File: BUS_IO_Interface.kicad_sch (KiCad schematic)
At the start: 20 parts, among them U26 DS28E83Q+T, U28 MAX31331TETB+, U29 MAX31725MTA+, U30 MAX31725MTA+, Y26 AB26T-32.768KHZ-6B

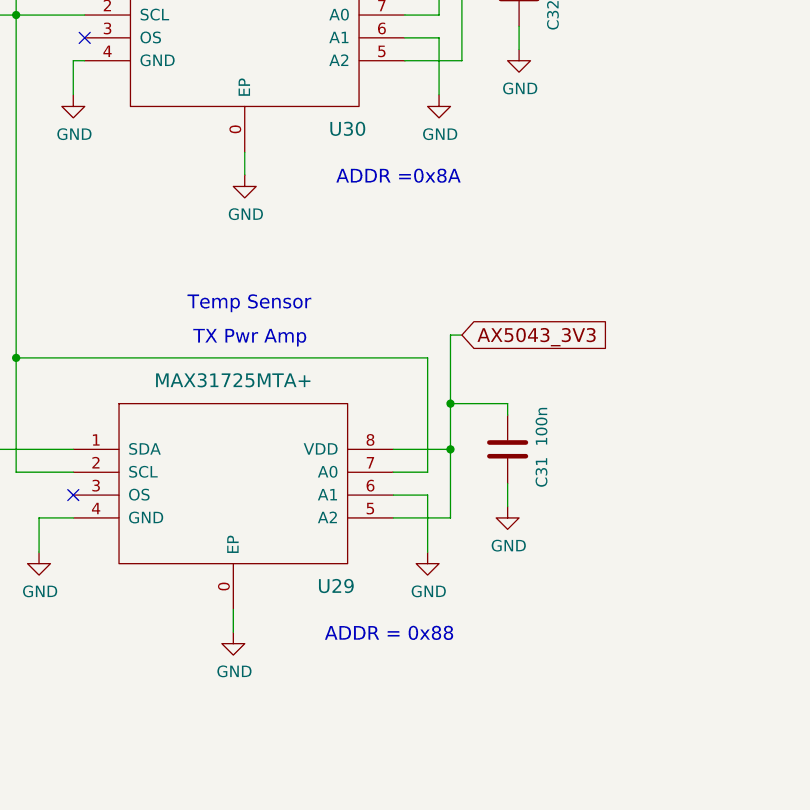
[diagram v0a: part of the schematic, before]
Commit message: Lots of cleanups to fix numerous issues
Signed-off-by: Corey Minyard <corey@minyard.net>
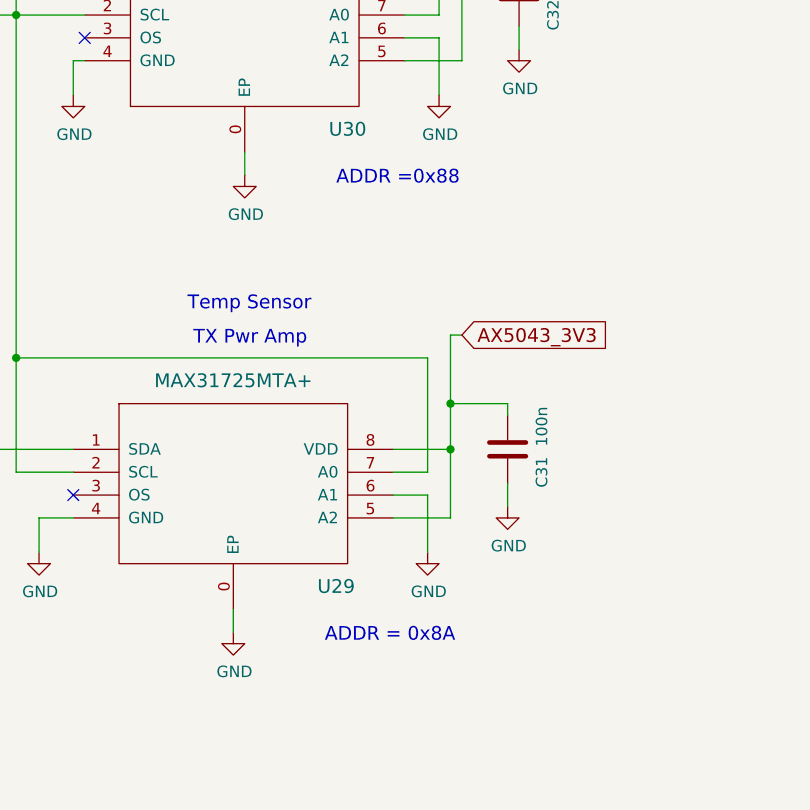
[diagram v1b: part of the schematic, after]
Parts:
- D26, D27: value RB521CS30L,315 -> RB521CS30L,315
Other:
- note added: "ADDR = 0x8A"
- note added: "ADDR =0x88"
- note removed: "ADDR = 0x88"
- note removed: "ADDR =0x8A"

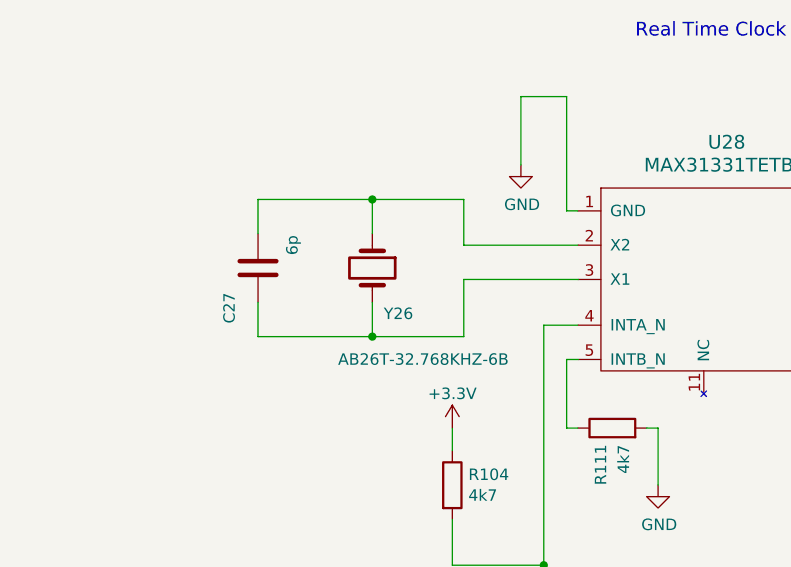
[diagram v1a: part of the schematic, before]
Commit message: Add notes file with todos and history, more cleanups
Signed-off-by: Corey Minyard <corey@minyard.net>
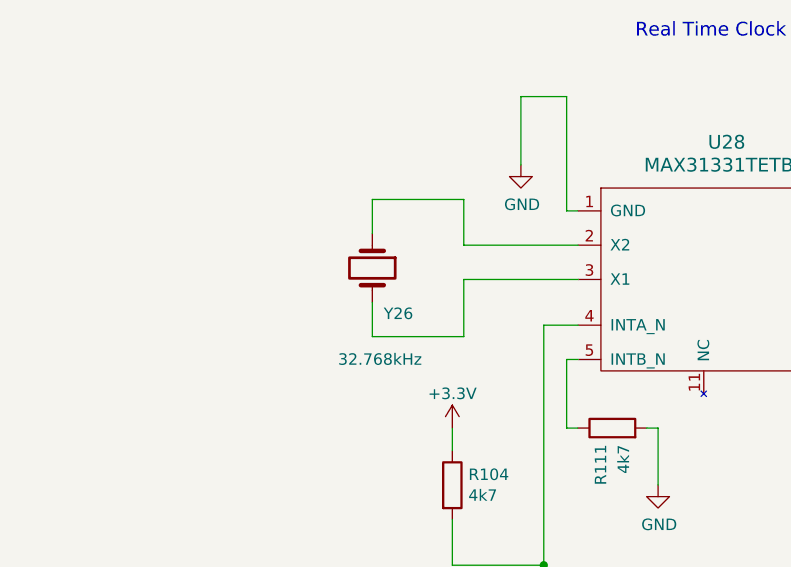
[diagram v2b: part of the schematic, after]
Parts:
- removed C27: 6p, Capacitor_SMD:C_0603_1608Metric_Pad1.08x0.95mm_HandSolder, symbol Device:C
- Y26: value AB26T-32.768KHZ-6B -> 32.768kHz; footprint Crystal:Crystal_AT310_D3.0mm_L10.0mm_Horizontal -> Crystal:Crystal_SMD_EuroQuartz_EQ161-2Pin_3.2x1.5mm
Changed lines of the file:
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@@
 	)
 	(junction
-		(at 71.12 146.05)
-		(diameter 0)
-		(color 0 0 0 0)
-	)
-	(junction
 		(at 303.53 121.92)
 		(diameter 0)
@@
 	)
 	(junction
-		(at 71.12 161.29)
-		(diameter 0)
-		(color 0 0 0 0)
-	)
-	(junction
 		(at 261.62 71.12)
 		(diameter 0)
@@
 	(wire
 		(pts
-			(xy 58.42 146.05) (xy 71.12 146.05)
-		)
-		(stroke
-			(width 0)
-			(type default)
-		)
-	)
-	(wire
-		(pts
 			(xy 255.27 124.46) (xy 261.62 124.46)
 		)
@@
 	(wire
 		(pts
-			(xy 58.42 161.29) (xy 71.12 161.29)
-		)
-		(stroke
-			(width 0)
-			(type default)
-		)
-	)
-	(wire
-		(pts
 			(xy 303.53 116.84) (xy 303.53 121.92)
 		)
@@
 	(wire
 		(pts
-			(xy 58.42 157.48) (xy 58.42 161.29)
-		)
-		(stroke
-			(width 0)
-			(type default)
-		)
-	)
-	(wire
-		(pts
 			(xy 123.19 82.55) (xy 123.19 85.09)
 		)
@@
 	(wire
 		(pts
-			(xy 58.42 149.86) (xy 58.42 146.05)
-		)
-		(stroke
-			(width 0)
-			(type default)
-		)
-	)
-	(wire
-		(pts
 			(xy 80.01 171.45) (xy 80.01 173.99)
 		)
@@
 			)
 		)
-		(property "Value" "AB26T-32.768KHZ-6B"
+		(property "Value" "32.768kHz"
 			(at 67.31 163.83 90)
 			(effects
@@
 			)
 		)
-		(property "Footprint" "Crystal:Crystal_AT310_D3.0mm_L10.0mm_Horizontal"
+		(property "Footprint" "Crystal:Crystal_SMD_EuroQuartz_EQ161-2Pin_3.2x1.5mm"
 			(at 71.12 153.67 0)
 			(effects
@@
 					(unit 1)
 				)
-			)
-		)
-	)
-	(symbol
-		(lib_id "Device:C")
-		(at 58.42 153.67 0)
-		(unit 1)
-		(exclude_from_sim no)
-		(in_bom yes)
-		(on_board yes)
-		(dnp no)
-		(property "Reference" "C27"
-			(at 55.245 158.115 90)
-			(effects
-				(font
-					(size 1.27 1.27)
-				)
-			)
-		)
-		(property "Value" "6p"
-			(at 62.23 151.13 90)
-			(effects
-				(font
-					(size 1.27 1.27)
-				)
-			)
-		)
-		(property "Footprint" "Capacitor_SMD:C_0603_1608Metric_Pad1.08x0.95mm_HandSolder"
-			(at 59.3852 157.48 0)
-			(effects
-				(font
-					(size 1.27 1.27)
-				)
-				(hide yes)
-			)
-		)
-		(property "Datasheet" "~"
-			(at 58.42 153.67 0)
-			(effects
-				(font
-					(size 1.27 1.27)
-				)
-			)
-		)
-		(property "Description" ""
-			(at 58.42 153.67 0)
-			(effects
-				(font
-					(size 1.27 1.27)
-				)
-			)
-		)
-		(pin "1"
-		)
-		(pin "2"
-		)
-		(instances
-			(project "PacSat_Dev_RevD_240614"
-				(path "/cc9f42d2-6985-41ac-acab-5ab7b01c5b38/aff81ec5-748c-4fc9-b1e8-df12a16f6289"
-					(reference "C27")
-					(unit 1)
-				)

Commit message: More hacking on things
Signed-off-by: Corey Minyard <corey@minyard.net>
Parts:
- removed C28: 470n, Capacitor_SMD:C_0603_1608Metric_Pad1.08x0.95mm_HandSolder, symbol Device:C
- removed C31, C32: 100n, Capacitor_SMD:C_0603_1608Metric_Pad1.08x0.95mm_HandSolder, symbol Device:C
- removed R126: 20K, Resistor_SMD:R_0603_1608Metric_Pad0.98x0.95mm_HandSolder, symbol Device:R
- removed R30, R31: 4k7, Resistor_SMD:R_0603_1608Metric_Pad0.98x0.95mm_HandSolder, symbol Device:R
- removed U26: DS28E83Q+T, PacSatDev_maxim:TDFN_T633_2, symbol PACSAT_ICs:DS28E83
- removed U29, U30: MAX31725MTA+, PacSatDev_maxim:TDFN_T833_2, symbol PACSAT_ICs:MAX31725
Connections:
- no-connect marks 3 -> 0
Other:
- note added: "Add Temp Sensor thermistors for TX power amp and processor, maybe more places."
- note removed: "ADDR = 0x8A"
- note removed: "ADDR =0x88"
- note removed: "AX5043 TX"
- note removed: "Idd 2.5 uA/600 uA"
- note removed: "Secure Authenticator"
- note removed: "TX Pwr Amp"
- note removed: "Temp Sensor"

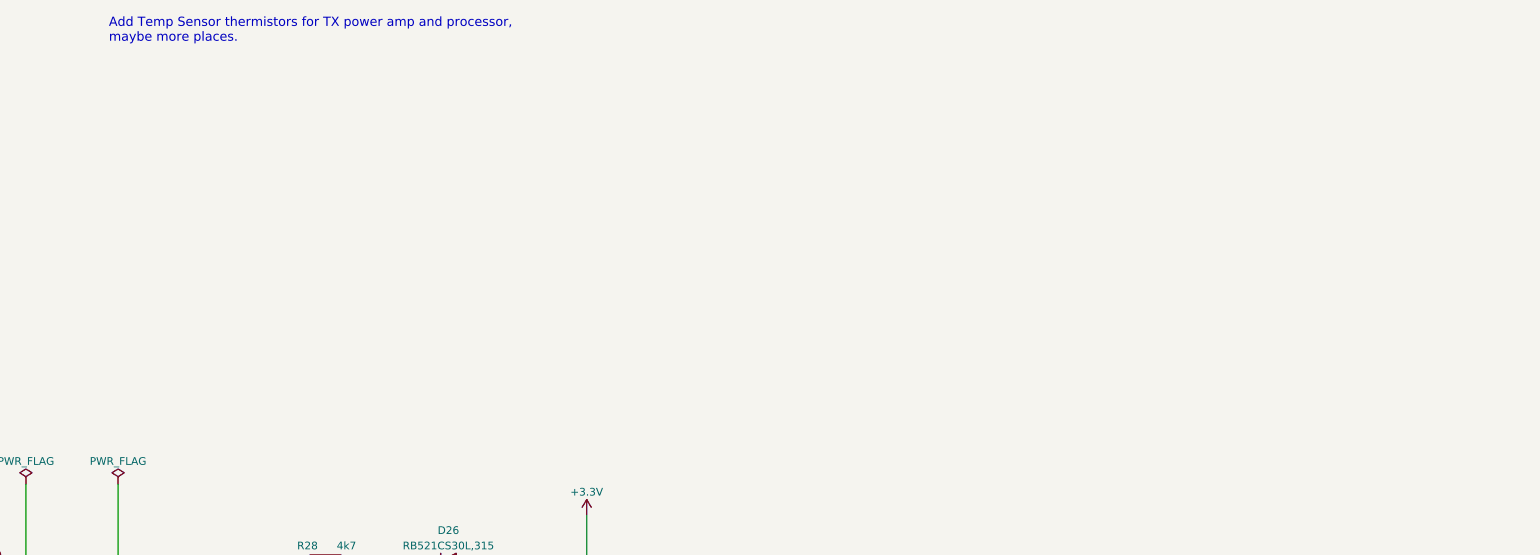
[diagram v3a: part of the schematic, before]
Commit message: Add resistors to the JTAG interface
They are supposed to be there.

Signed-off-by: Corey Minyard <corey@minyard.net>
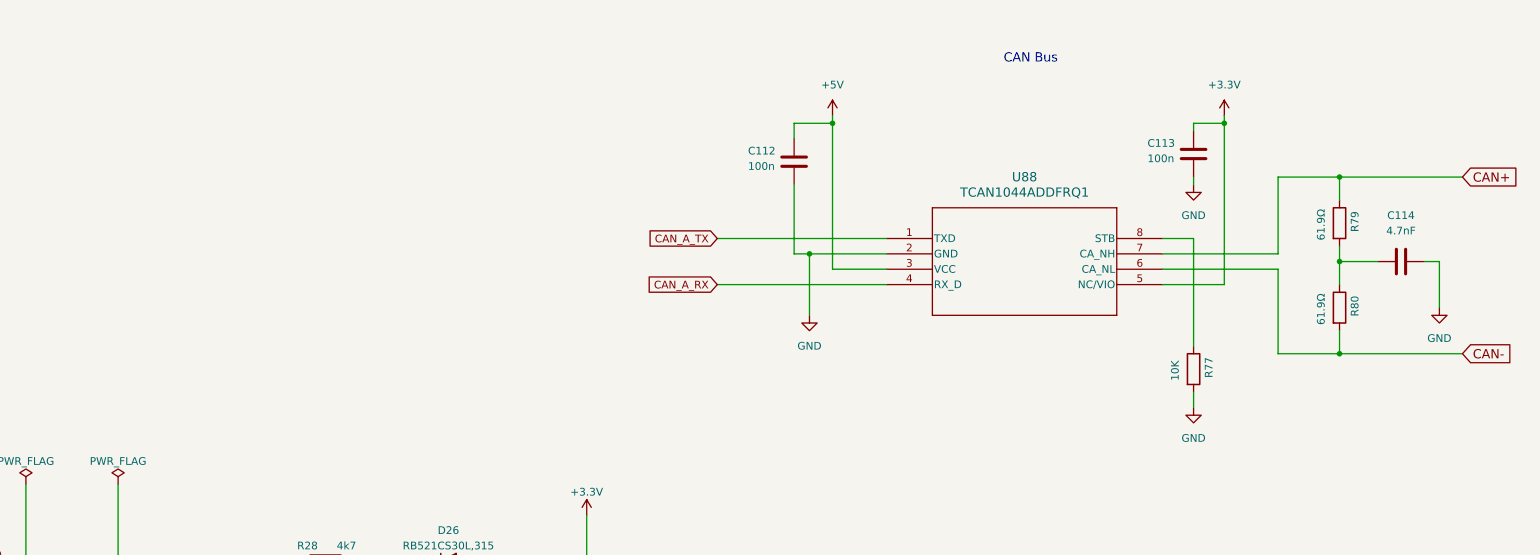
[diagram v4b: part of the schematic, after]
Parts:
- added C112, C113: 100n, Capacitor_SMD:C_0603_1608Metric_Pad1.08x0.95mm_HandSolder, symbol Device:C
- added C114: 4.7nF, Capacitor_SMD:C_0603_1608Metric_Pad1.08x0.95mm_HandSolder, symbol Device:C
- added R77: 10K, Resistor_SMD:R_0603_1608Metric_Pad0.98x0.95mm_HandSolder, symbol Device:R
- added R79, R80: 61.9Ω, Resistor_SMD:R_0603_1608Metric_Pad0.98x0.95mm_HandSolder, symbol Device:R
- added U88: TCAN1044ADDFRQ1, Package_TO_SOT_SMD:TSOT-23-8, symbol PACSAT_ICs:TCAN1044ADDFRQ1
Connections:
- net +3.3V: now also C113.1, U88.5 (NC/VIO)
- net GND: now also C112.2, C113.2, C114.2, R77.2, U88.2 (GND)
- new net: C114.1, R79.2, R80.1
- new net: R77.1, U88.8 (STB)
- new net +5V: C112.1, U88.3 (VCC)
- new net CAN+: R79.1, U88.7 (CA_NH)
- new net CAN-: R80.2, U88.6 (CA_NL)
- new net CAN_A_RX: U88.4 (RX_D)
- new net CAN_A_TX: U88.1 (TXD)
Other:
- note added: "CAN Bus"
- note removed: "Add Temp Sensor thermistors for TX power amp and processor, maybe more places."

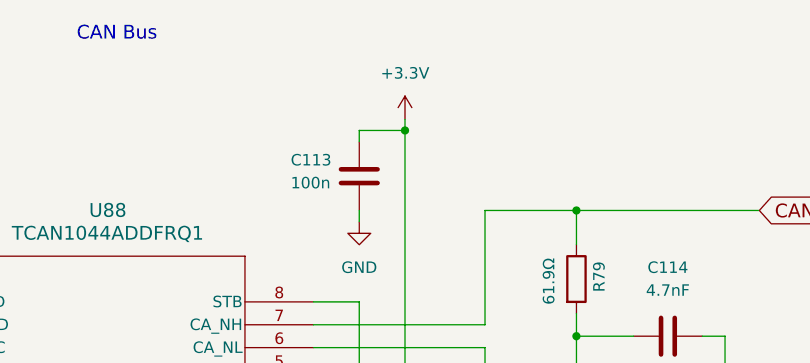
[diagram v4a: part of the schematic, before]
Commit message: Rework the AX5043 RX side to a different balun
It's cheaper (though not smaller) and fits inside the shield.

Signed-off-by: Corey Minyard <corey@minyard.net>
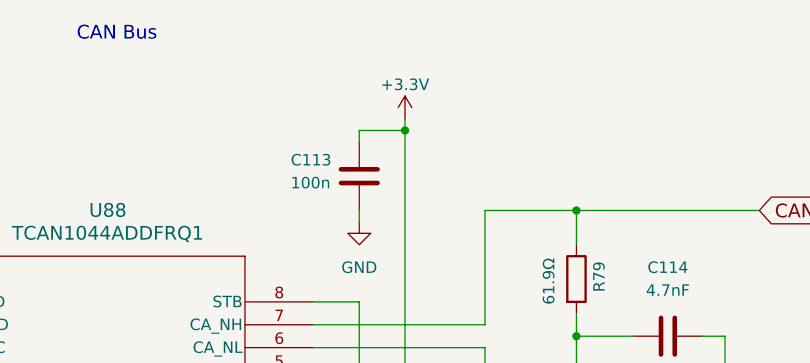
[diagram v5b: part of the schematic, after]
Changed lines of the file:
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@@
+	)
+	(symbol
+		(lib_id "power:+3.3V")
+		(at 328.93 72.39 0)
+		(unit 1)
+		(exclude_from_sim no)
+		(in_bom yes)
+		(on_board yes)
+		(dnp no)
+		(fields_autoplaced yes)
+		(property "Reference" "#PWR0164"
+			(at 328.93 76.2 0)
+			(effects
+				(font
+					(size 1.27 1.27)
+				)
+				(hide yes)
+			)
+		)
+		(property "Value" "+3.3V"
+			(at 328.93 68.58 0)
+			(effects
+				(font
+					(size 1.27 1.27)
+				)
+			)
+		)
+		(property "Footprint" ""
+			(at 328.93 72.39 0)
+			(effects
+				(font
+					(size 1.27 1.27)
+				)
+				(hide yes)
+			)
+		)
+		(property "Datasheet" ""
+			(at 328.93 72.39 0)
+			(effects
+				(font
+					(size 1.27 1.27)
+				)
+				(hide yes)
+			)
+		)
+		(property "Description" ""
+			(at 328.93 72.39 0)
+			(effects
+				(font
+					(size 1.27 1.27)
+				)
+			)
+		)
+		(pin "1"
+		)
+		(instances
+			(project "PacSat_AFSK"
+				(path "/cc9f42d2-6985-41ac-acab-5ab7b01c5b38/aff81ec5-748c-4fc9-b1e8-df12a16f6289"
+					(reference "#PWR0164")
+					(unit 1)
+				)
+			)
+		)
 	)
 	(symbol
@@
 					(unit 1)
 				)
-			)
-		)
-	)
-	(symbol
-		(lib_id "LocalPower:VIO")
-		(at 328.93 72.39 0)
-		(unit 1)
-		(exclude_from_sim no)
-		(in_bom yes)
-		(on_board yes)
-		(dnp no)
-		(fields_autoplaced yes)
-		(property "Reference" "#PWR0164"
-			(at 328.93 76.2 0)
-			(effects
-				(font
-					(size 1.27 1.27)
-				)
-				(hide yes)
-			)
-		)
-		(property "Value" "+3.3V"
-			(at 328.93 67.31 0)
-			(effects
-				(font
-					(size 1.27 1.27)
-				)
-			)
-		)
-		(property "Footprint" ""
-			(at 328.93 72.39 0)
-			(effects
-				(font
-					(size 1.27 1.27)
-				)
-				(hide yes)
-			)
-		)
-		(property "Datasheet" ""
-			(at 328.93 72.39 0)
-			(effects
-				(font
-					(size 1.27 1.27)
-				)
-				(hide yes)
-			)
-		)
-		(property "Description" "Power symbol creates a global label with name \"+3.3VA\""
-			(at 328.93 72.39 0)
-			(effects
-				(font
-					(size 1.27 1.27)
-				)
-				(hide yes)
-			)
-		)
-		(pin "1"
-		)
-		(instances
-			(project "PacSat_AFSK"
-				(path "/cc9f42d2-6985-41ac-acab-5ab7b01c5b38/aff81ec5-748c-4fc9-b1e8-df12a16f6289"
-					(reference "#PWR0164")
-					(unit 1)
-				)

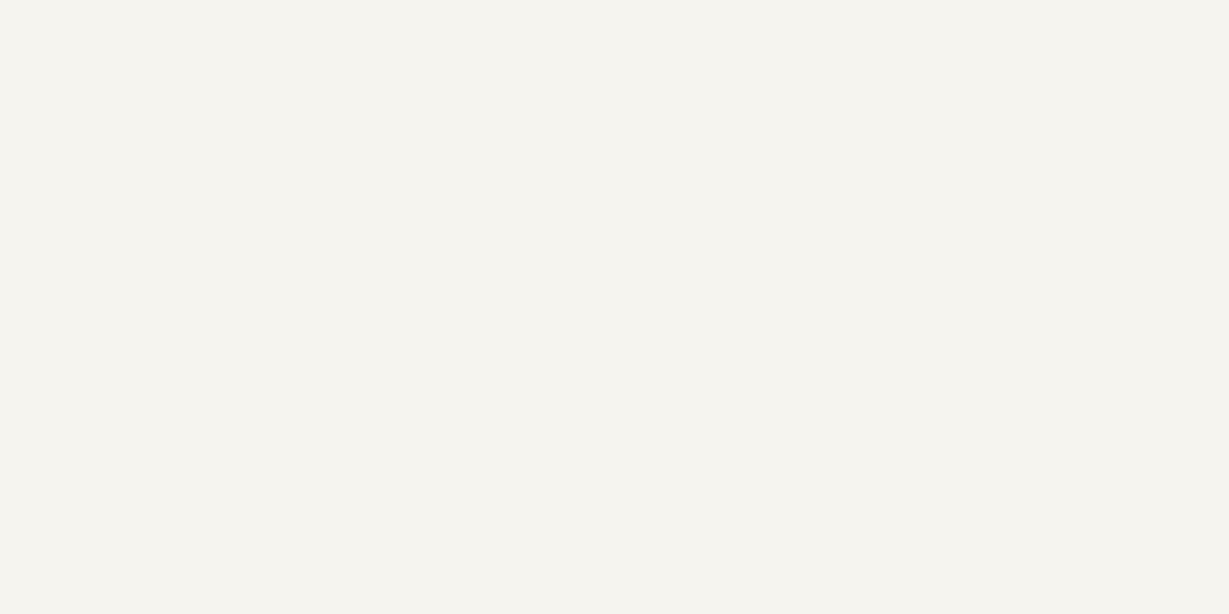
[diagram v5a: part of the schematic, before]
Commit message: Rework hierarchical sheets
Signed-off-by: Corey Minyard <corey@minyard.net>
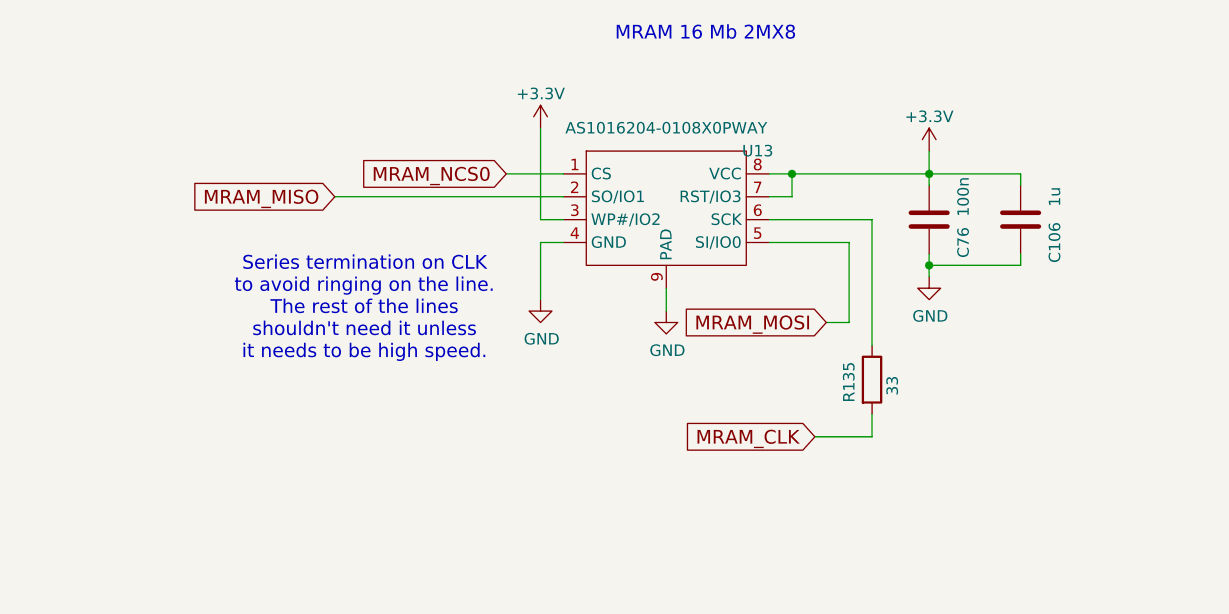
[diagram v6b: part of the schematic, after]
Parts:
- added C106: 1u, Capacitor_SMD:C_0603_1608Metric_Pad1.08x0.95mm_HandSolder, symbol Device:C
- added C76: 100n, Capacitor_SMD:C_0603_1608Metric_Pad1.08x0.95mm_HandSolder, symbol Device:C
- added R135: 33, Resistor_SMD:R_0603_1608Metric_Pad0.98x0.95mm_HandSolder, symbol Device:R
- added U13: AS1016204-0108X0PWAY, Package_SON:WSON-8-1EP_8x6mm_P1.27mm_EP3.4x4.3mm, symbol PACSAT_ICs:QSPI_FLASH_WSON_8-pin
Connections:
- net +3.3V: now also C106.1, C76.1, U13.3 (WP#/IO2), U13.7 (RST/IO3), U13.8 (VCC)
- net GND: now also C106.2, C76.2, U13.4 (GND), U13.9 (PAD)
- new net: R135.1, U13.6 (SCK)
- new net MRAM_CLK: R135.2
- new net MRAM_MISO: U13.2 (SO/IO1)
- new net MRAM_MOSI: U13.5 (SI/IO0)
- new net MRAM_NCS0: U13.1 (CS)
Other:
- note added: "MRAM 16 Mb 2MX8"
- note added: "Series termination on CLK to avoid ringing on the line. The rest of the lines shouldn't need it unless it needs to be high speed."
